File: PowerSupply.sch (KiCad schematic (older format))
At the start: 10 parts

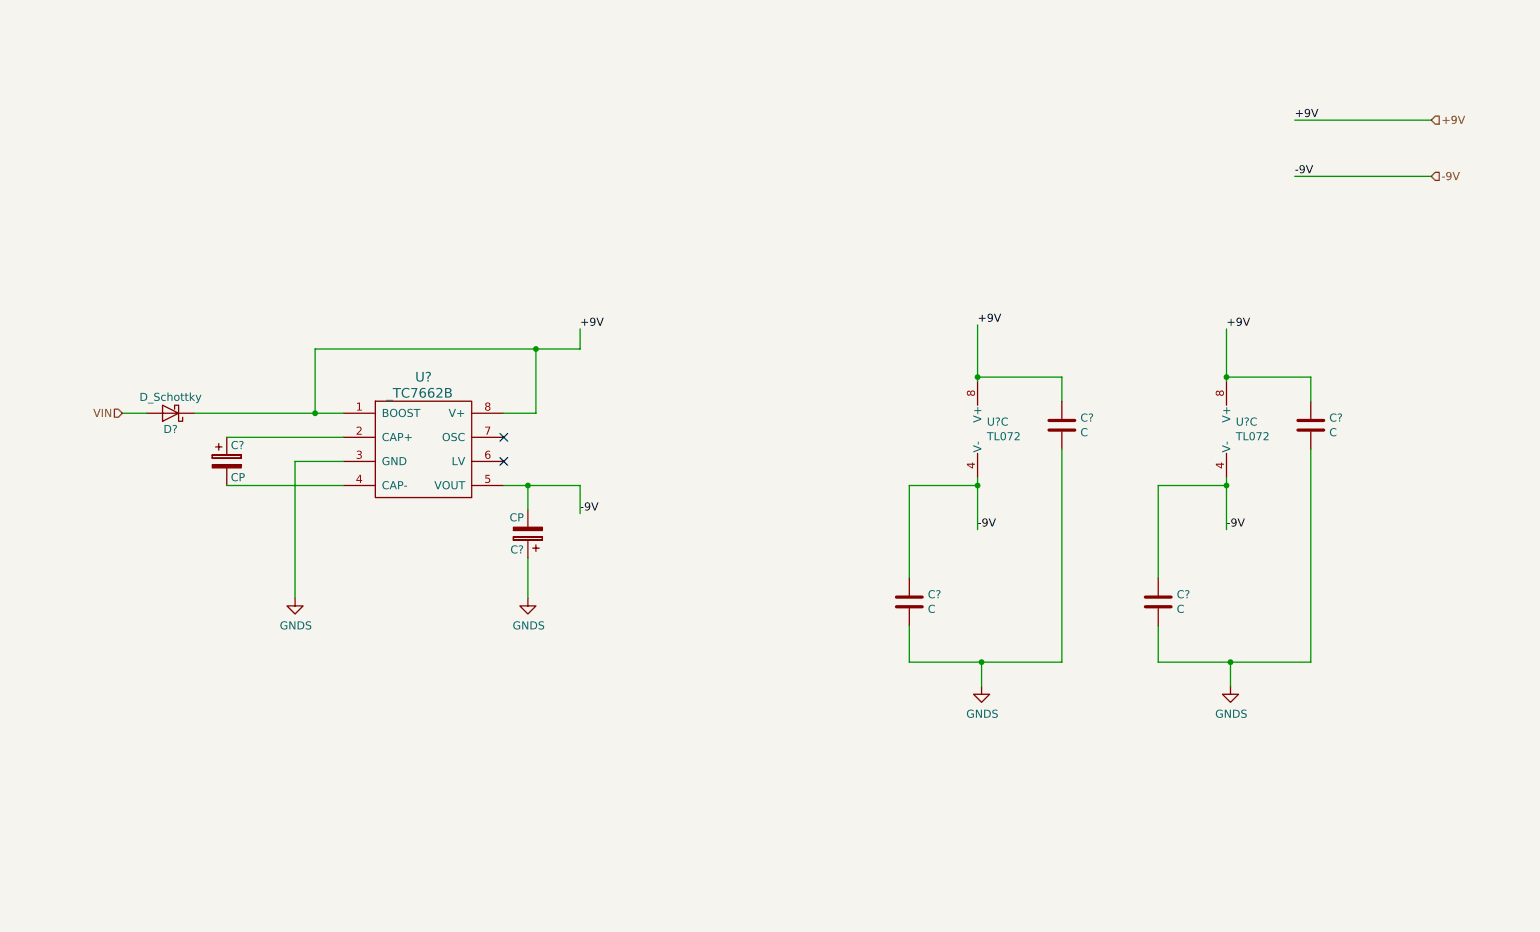
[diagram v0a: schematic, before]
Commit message: Updated power supply section
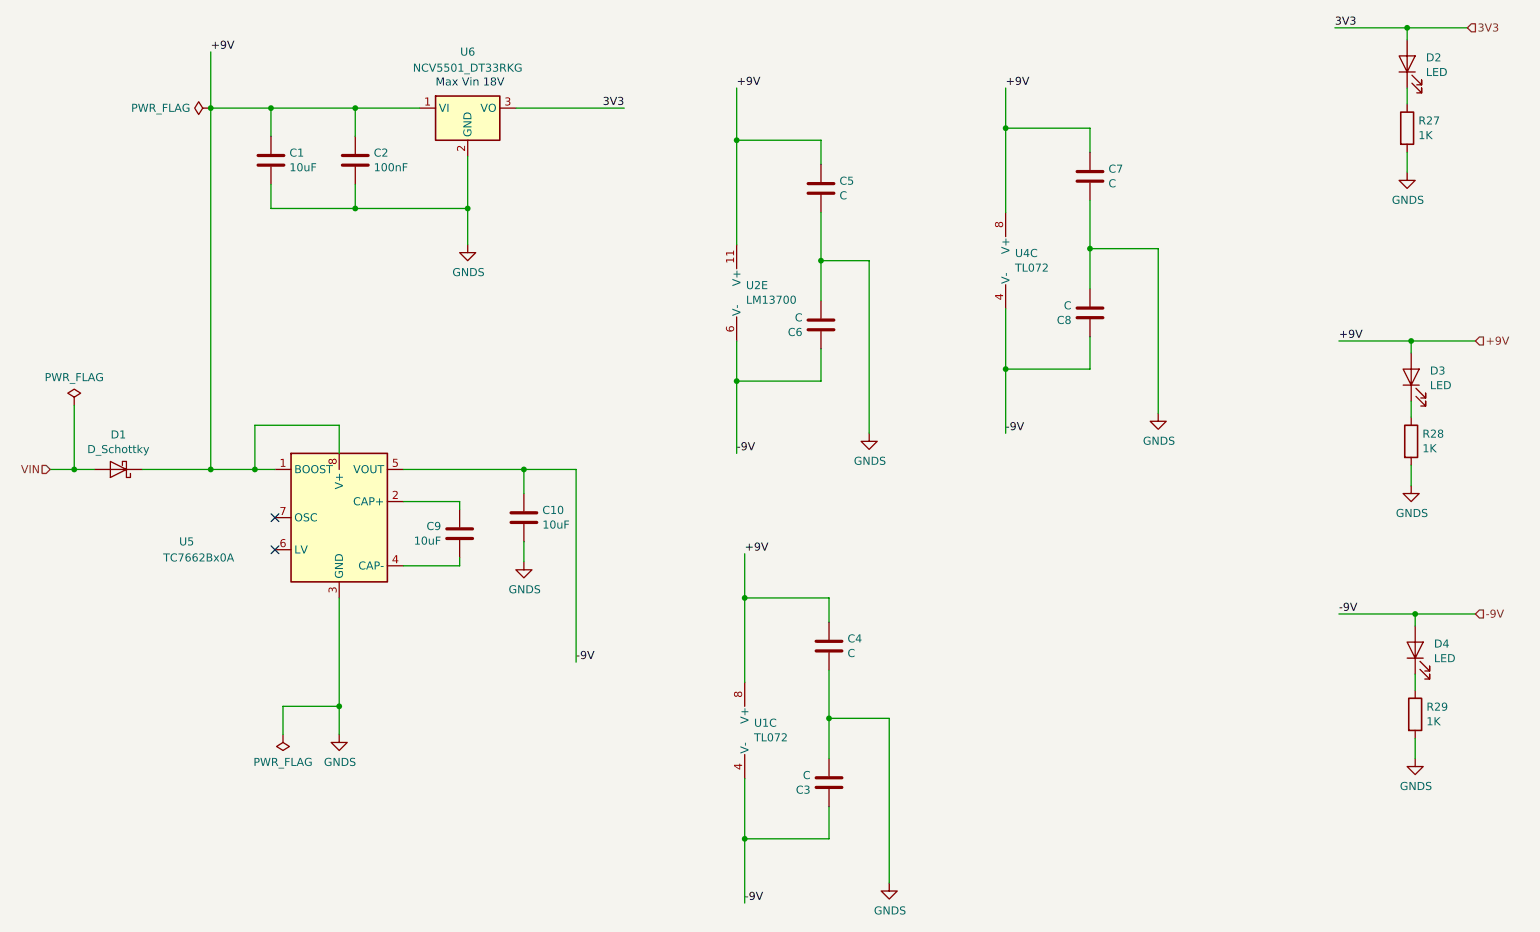
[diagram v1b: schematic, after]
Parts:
- removed C? (x2): CP, symbol Digital_OTA_Tremolo-rescue:CP
- removed C? (x2): C, symbol Device:C
- removed D?: D_Schottky, symbol Digital_OTA_Tremolo-rescue:D_Schottky
- removed U?: _TC7662B, symbol _TC7662b:_TC7662B
- added C1, C10, C9: 10uF, symbol Device:C
- added C2: 100nF, symbol Device:C
- added C5, C6, C7, C8: C, symbol Device:C
- added D1: D_Schottky, symbol Device:D_Schottky
- added D2, D3, D4: LED, symbol Device:LED
- added R27, R28, R29: 1K, symbol Device:R
- added U2: LM13700, symbol Amplifier_Operational:LM13700
- added U5: TC7662Bx0A, Package_SO:SOIC-8_3.9x4.9mm_P1.27mm, symbol Converter_DCDC:TC7662Bx0A
- added U6: NCV5501_DT33RKG, Package_TO_SOT_SMD:TO-252-3_TabPin2, symbol Regulator_Linear:MCP1825S
- gave numbers to parts that had none: 4
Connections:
- net +9V: now also C1.1, C2.1, C5.1, C7.1, D1.1 (K), D3.2 (A), U2.11 (V+), U5.1 (BOOST), U5.8 (V+), U6.1 (VI)
- net -9V: now also C10.1, C6.1, C8.1, D4.2 (A), U2.6 (V-), U5.5 (VOUT)
- net GNDS: now also C1.2, C10.2, C2.2, C5.2, C6.2, C7.2, C8.2, R27.2, R28.2, R29.2, U5.3 (GND), U6.2 (GND)
- net VIN: now also D1.2 (A)
- new net: C9.1, U5.2 (CAP+)
- new net: C9.2, U5.4 (CAP-)
- new net: D2.1 (K), R27.1
- new net: D3.1 (K), R28.1
- new net: D4.1 (K), R29.1
- new net 3V3: D2.2 (A), U6.3 (VO)
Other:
- note added: "Max Vin 18V"
- moved on the sheet: C3, C4, U1C, U4C

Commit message: Updated RevA design
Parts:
- removed C10, C9: 10uF, symbol Device:C
- removed C3, C4: C, symbol Device:C
- removed U1, U4: TL072, symbol Amplifier_Operational:TL072
- removed U5: TC7662Bx0A, Package_SO:SOIC-8_3.9x4.9mm_P1.27mm, symbol Converter_DCDC:TC7662Bx0A
- added U1: TL074, Package_SO:SOIC-16_3.9x9.9mm_P1.27mm, symbol Amplifier_Operational:TL074
- added U5: RS6-0515D, RecomRS6:RS6, symbol RecomRS6:RS6-xxxxD
- C1, C2: footprint (none) -> Capacitor_SMD:C_0805_2012Metric_Pad1.15x1.40mm_HandSolder
- C5, C6, C7, C8: value C -> 100nF; footprint (none) -> Capacitor_SMD:C_0805_2012Metric_Pad1.15x1.40mm_HandSolder
- D1: footprint (none) -> Diode_SMD:D_SMA_Handsoldering
- D2, D3, D4: footprint (none) -> LED_SMD:LED_1206_3216Metric_Pad1.42x1.75mm_HandSolder
- R27, R28, R29: footprint (none) -> Resistor_SMD:R_0805_2012Metric_Pad1.15x1.40mm_HandSolder
- U2: footprint (none) -> Package_SO:SOIC-16_3.9x9.9mm_P1.27mm
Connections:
- net +9V: no longer names the net of C1.1, C2.1, D1.1 (K), U6.1 (VI)
- net +9V: now also U5.2 (+Vin); no longer C5.1, C7.1, D3.2 (A), U2.11 (V+)
- net -9V renamed -15V
- net -15V: now also U1.11 (V-), U5.8 (-Vout)
- net GNDS renamed VCOM
- net VCOM: now also U5.7 (COM)
- net VIN renamed +VIN
- new net +15V: C5.1, C7.1, D3.2 (A), U1.4 (V+), U2.11 (V+), U5.6 (+Vout)
- new net -VIN: U5.1 (-Vin)
- no-connect marks 2 -> 1
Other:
- moved on the sheet: D1, D2, D3, R27, R28
